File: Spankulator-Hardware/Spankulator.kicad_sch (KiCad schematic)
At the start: 103 parts, among them J1 3.5mm Jack, J12 Arduino Socket, J13 Arduino Socket, J2 Euro Power, J3 3.5mm Jack, J4 3.5mm Jack, J5 3.5mm Jack, J6 3.5mm Jack, J7 Expansion Header, J8 FRAM Header, J9 Display Header, Q2 VP2106, Q3 TN2106, Q4 VP2106, Q5 TN2106, Q7 TN2106, Q8 TN2106, SW1 Adj, SW2 Push Button, SW3 Push Button, SW4 Push Button, SW5 Push Button, SW6 Push Button, SW7 Push Button, SW8 Push Button, U1 TL032CP, U2 CD4013BE, U3 TL032CP, U4 MC78L05_TO92, U5 LP2950-3.3_TO92, U6 MAX7480

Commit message: Release 1.0
Full package.
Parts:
- C10, C8: Digi-Key Part 445-180204-ND -> 399-9886-1-ND
- C14: footprint Capacitor_THT:C_Rect_L4.6mm_W2.0mm_P2.50mm_MKS02_FKP02 -> Capacitor_THT:C_Rect_L7.0mm_W2.0mm_P5.00mm; Digi-Key Part 445-180204-ND -> 399-9886-1-ND
- Q3, Q5, Q7, Q8: value TN2106 -> 2N7000TA; Digi-Key Part TN2106N3-G-ND -> 2N7000TACT-ND; LCSC Part # C258163 -> C107290
- U4: LCSC Part # (none) -> C156437
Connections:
- net +3V3: now also C9.1
- net +5V: no longer C9.1
- net -12V: now also C9.2
- net GND: no longer C9.2
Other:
- note added: "LCSC: VP0808"
- note added: "Stuff U1 last after installing RV2. LCSC Part# omitted intentionally."
- moved on the sheet: C15, C7, C8, C9, TP1, TP2, U4

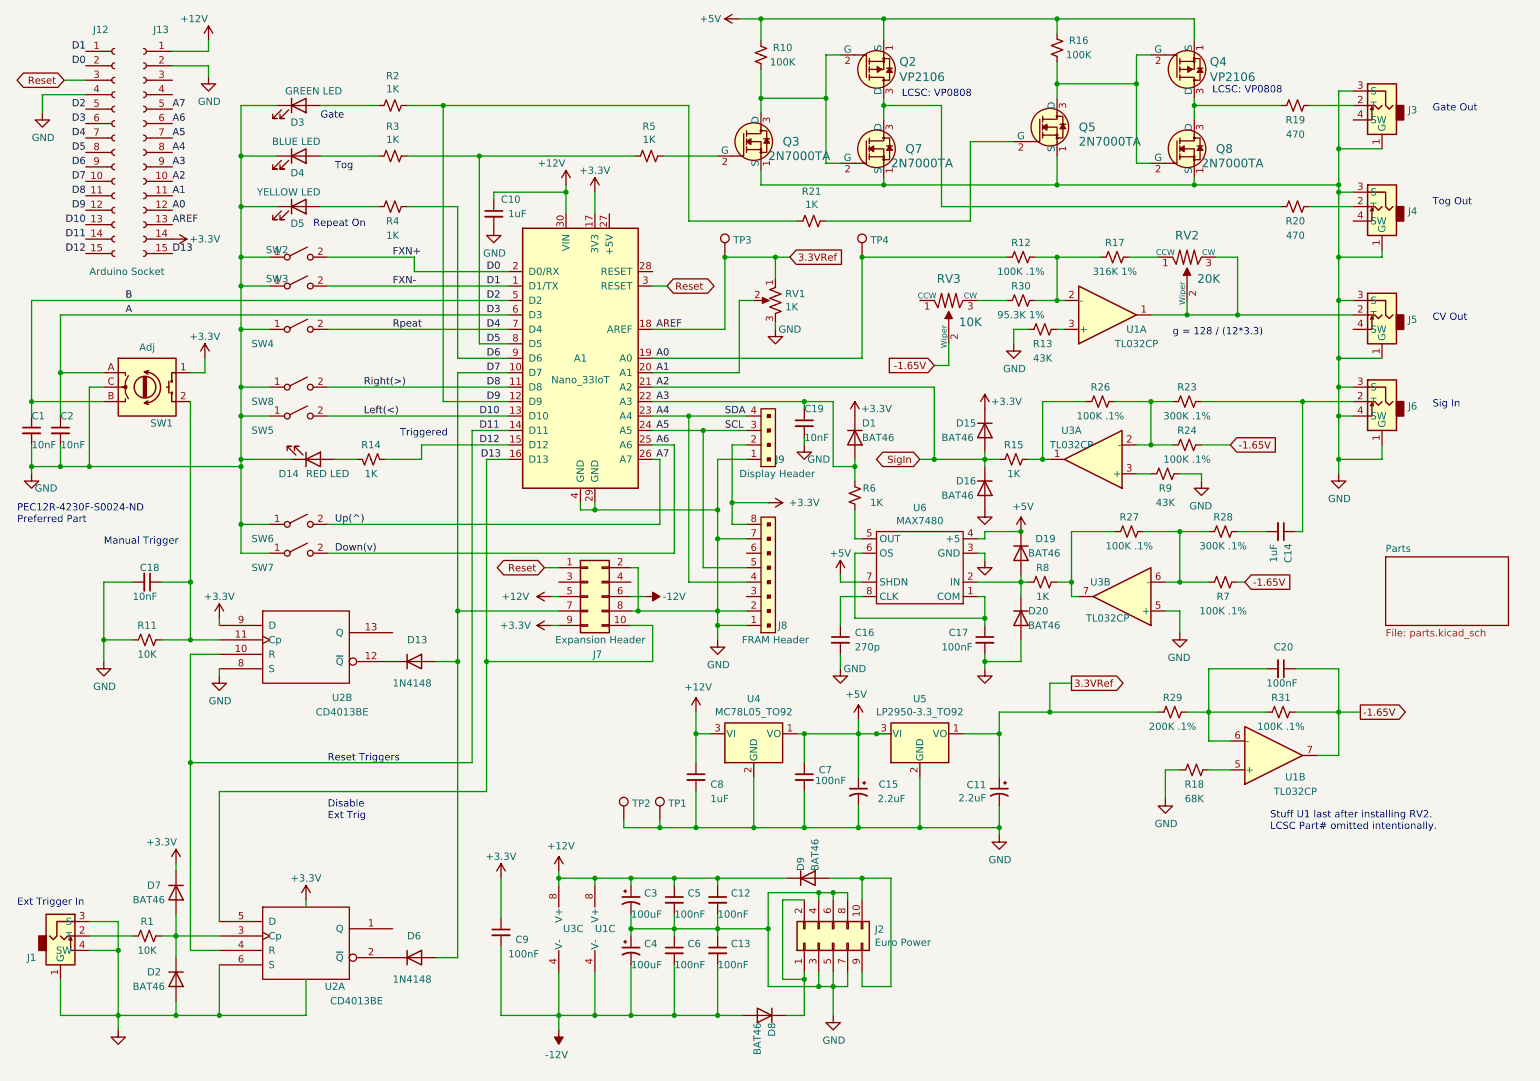
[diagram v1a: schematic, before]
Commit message: Adds DuDad. Updates Excel to use Power Query.
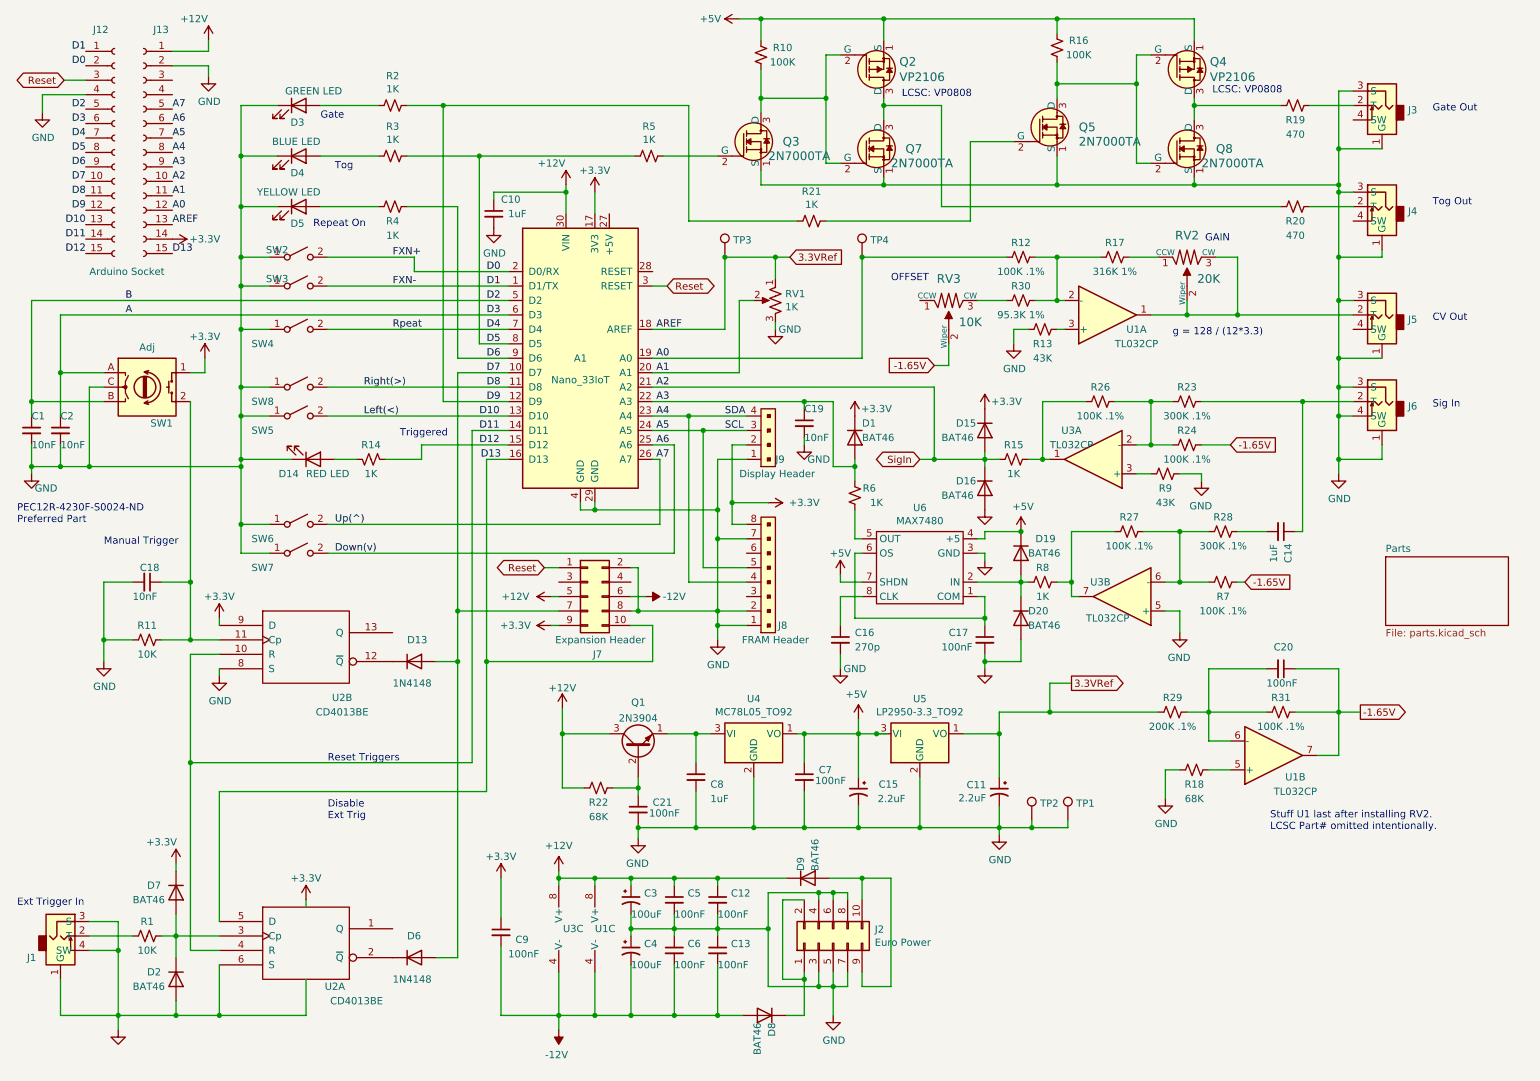
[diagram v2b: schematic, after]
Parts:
- added C21: 100nF, Capacitor_THT:C_Rect_L7.0mm_W2.0mm_P5.00mm, symbol Device:C_Small
- added Q1: 2N3904, digikey-footprints:TO-92-3_Formed_Leads, symbol Transistor_BJT:2N3904
- added R22: 68K, Resistor_THT:R_Axial_DIN0207_L6.3mm_D2.5mm_P10.16mm_Horizontal, symbol Device:R_Small_US
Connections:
- net +12V: now also Q1.3 (C), R22.2; no longer C8.1, U4.3 (VI)
- net GND: now also C21.2
- new net: C8.1, Q1.1 (E), U4.3 (VI)
- new net: C21.1, Q1.2 (B), R22.1
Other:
- note added: "GAIN"
- note added: "OFFSET"
- moved on the sheet: TP1, TP2

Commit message: Consolidates zip_gerbers.bat. Improves BOM files.
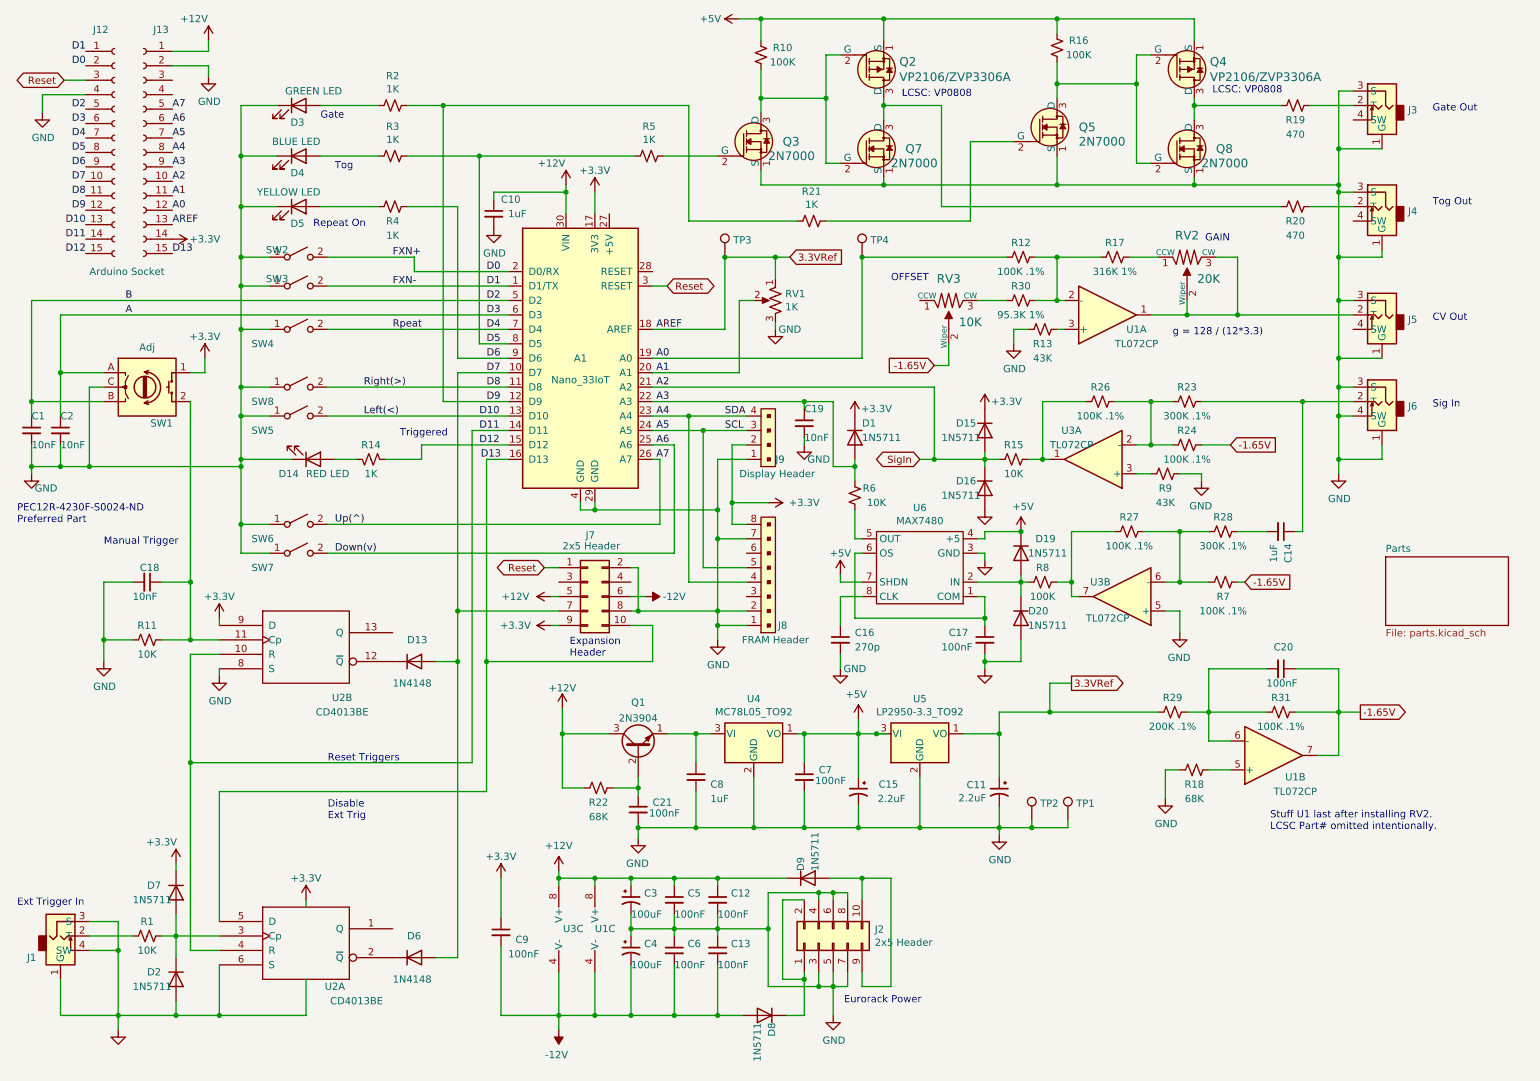
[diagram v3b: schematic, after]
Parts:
- D1, D15, D16, D19, D2, D20, D7, D8, D9: value BAT46 -> 1N5711; Digi-Key Part BAT46CT-ND -> 497-2499-1-ND; LCSC Part # C2798198 -> C283247
- J2: value Euro Power -> 2x5 Header
- J7: value Expansion Header -> 2x5 Header
- Q2, Q4: value VP2106 -> VP2106/ZVP3306A; LCSC Part # C632609 -> C211372
- Q3, Q5, Q7, Q8: value 2N7000TA -> 2N7000; LCSC Part # C107290 -> C9114
- R12, R24, R26, R27, R31, R7: LCSC Part # C511595 -> C410694
- R15, R6: value 1K -> 10K; Digi-Key Part CF14JT1K00CT-ND -> CF14JT10K0CT-ND; LCSC Part # C66649 -> C433778
- R18, R22: LCSC Part # C479260 -> C70783
- R8: value 1K -> 100K; Digi-Key Part CF14JT1K00CT-ND -> 2019-CF1/4CT52R104JCT-ND; LCSC Part # C66649 -> C120103
- U1: value TL032CP -> TL072CP; Build Type (none) -> delete; Digi-Key Part 296-7149-5-ND -> 296-1775-5-ND
- U2: Build Type (none) -> full
- U3: value TL032CP -> TL072CP; footprint Package_DIP:DIP-8_W7.62mm -> digikey-footprints:DIP-8_W7.62mm; Digi-Key Part 296-7149-5-ND -> 296-1775-5-ND
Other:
- note added: "Eurorack Power"
- note added: "Expansion Header"

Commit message: Adds Arduino headers to lcsc bom
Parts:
- J12, J13: LCSC Part # (none) -> C2932676
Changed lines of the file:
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@@
+      (effects (font (size 1.27 1.27)) hide)
+    )
+    (property "LCSC Part #" "C2932676" (id 5) (at 32.385 37.465 0)
       (effects (font (size 1.27 1.27)) hide)
     )
@@
       (effects (font (size 1.27 1.27)) hide)
     )
+    (property "LCSC Part #" "C2932676" (id 5) (at 37.465 37.465 0)
+      (effects (font (size 1.27 1.27)) hide)
+    )

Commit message: v4.4 of Spankulator Board
Many changes to BOM generation. Adds Python scripts.
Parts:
- C1, C10, C12, C13, C14, C17, C18, C19, C2, C21, C5, C6, C7, C8, C9: footprint Capacitor_THT:C_Rect_L7.0mm_W2.0mm_P5.00mm -> Capacitor_THT:C_Disc_D4.3mm_W1.9mm_P5.00mm
- C16: footprint Capacitor_THT:C_Rect_L4.0mm_W2.5mm_P2.50mm -> Capacitor_THT:C_Disc_D5.0mm_W2.5mm_P5.00mm
- C20: footprint Capacitor_THT:C_Rect_L7.0mm_W2.0mm_P5.00mm -> Capacitor_THT:C_Disc_D4.3mm_W1.9mm_P5.00mm; Build Type (none) -> split; LCSC Part # C400087 -> (none)
- C3, C4: LCSC Part # (none) -> C88859
- D8: footprint Diode_THT:D_DO-35_SOD27_P7.62mm_Horizontal -> Diode_THT:D_DO-35_SOD27_P2.54mm_Vertical_AnodeUp
- D9: footprint Diode_THT:D_DO-35_SOD27_P7.62mm_Horizontal -> Diode_THT:D_DO-35_SOD27_P2.54mm_Vertical_KathodeUp
- J12, J13: LCSC Part # C2932676 -> (none)
- R16, R30, R31: footprint Resistor_THT:R_Axial_DIN0207_L6.3mm_D2.5mm_P10.16mm_Horizontal -> Resistor_THT:R_Axial_DIN0207_L6.3mm_D2.5mm_P2.54mm_Vertical
- RV2: URL (none) -> https://www.amazon.com/dp/B015RK03LI?psc=1&ref=ppx_yo2ov_dt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
- U1: footprint Package_DIP:DIP-8_W7.62mm -> Package_DIP:DIP-8_W7.62mm_Socket; Build Type delete -> split; LCSC Part # (none) -> C72124
- U2: Build Type full -> split
- U3: footprint digikey-footprints:DIP-8_W7.62mm -> Package_DIP:DIP-8_W7.62mm_Socket; Build Type (none) -> split
- U6: Build Type (none) -> split
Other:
- note removed: "Stuff U1 last after installing RV2. LCSC Part# omitted intentionally."

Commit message: Finish update to 5.0
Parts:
- removed J8: FRAM Header, sputterizer:PinHeader_1x8_P2.54mm_Drill1.02mm, symbol dk_Rectangular-Connectors-Headers-Male-Pins:8PINHeader
- added U7: MB85RC256, Package_SO:SOIC-8_3.9x4.9mm_P1.27mm, symbol Memory_NVRAM:FM24C64B
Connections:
- net +3V3: now also U7.8 (VDD)
- net A4: now also U7.5 (SDA)
- net A5: now also U7.6 (SCL)
- net GND: now also U7.4 (VSS)
- net A6 renamed Dn
- net A7 renamed Up
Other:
- moved on the sheet: SW6, SW7
